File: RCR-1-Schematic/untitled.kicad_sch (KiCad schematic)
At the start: 24 parts, among them J1 AC In, SW1 Chassis Safety, T1A Transformer_1P_SS, T1B Transformer_1P_2S

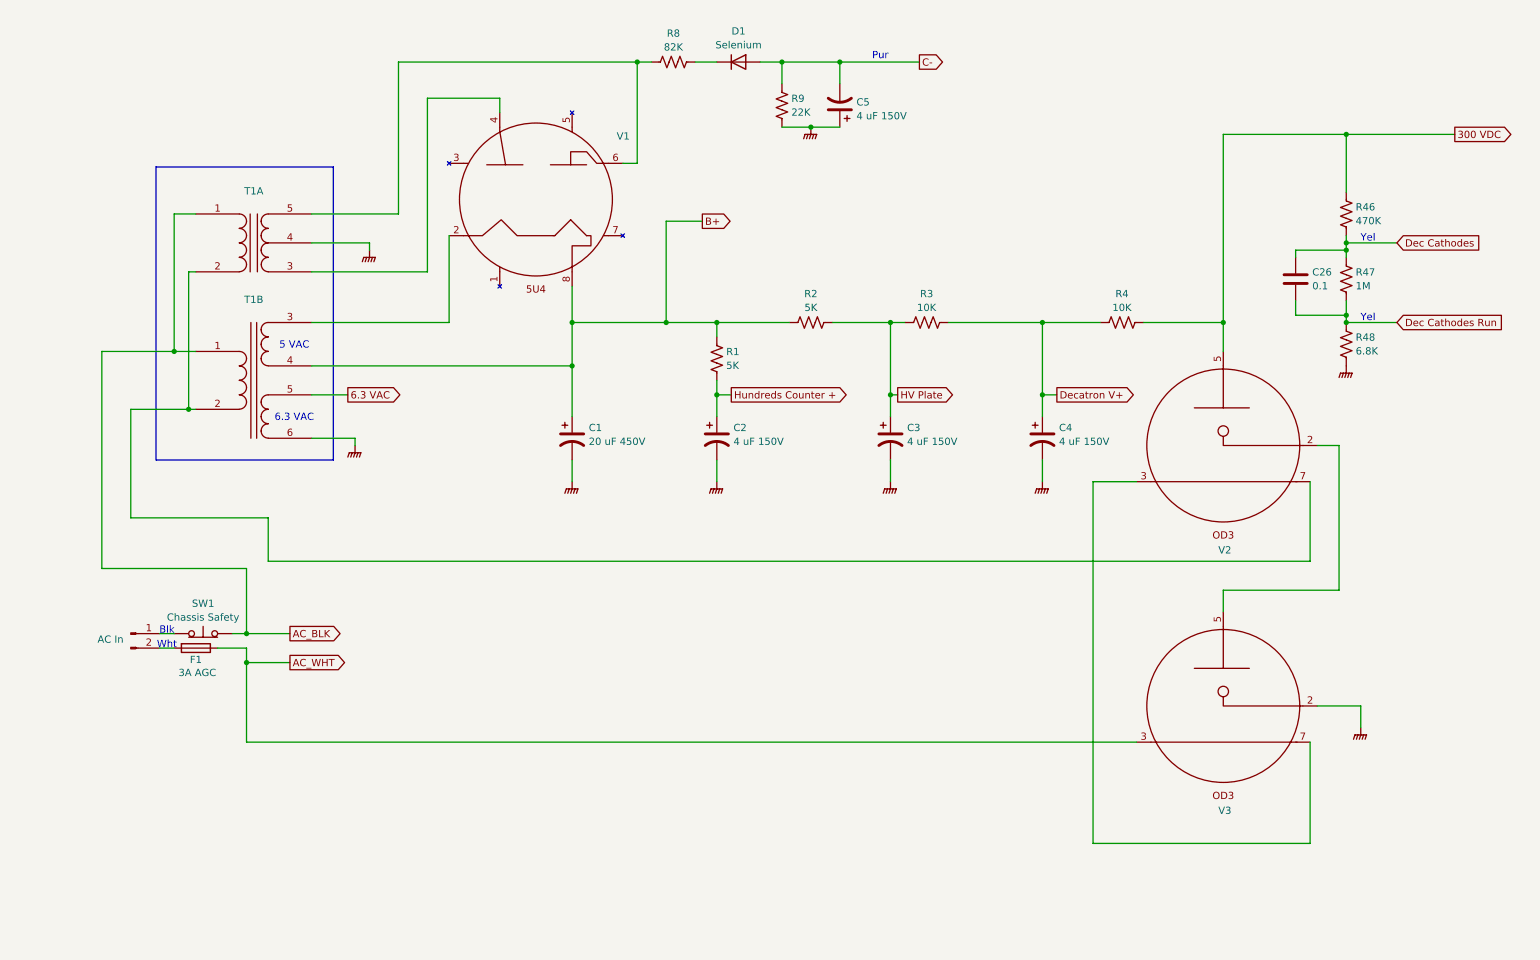
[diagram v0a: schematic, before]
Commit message: Add some oscilloscope screenshots, fixed some mistakes
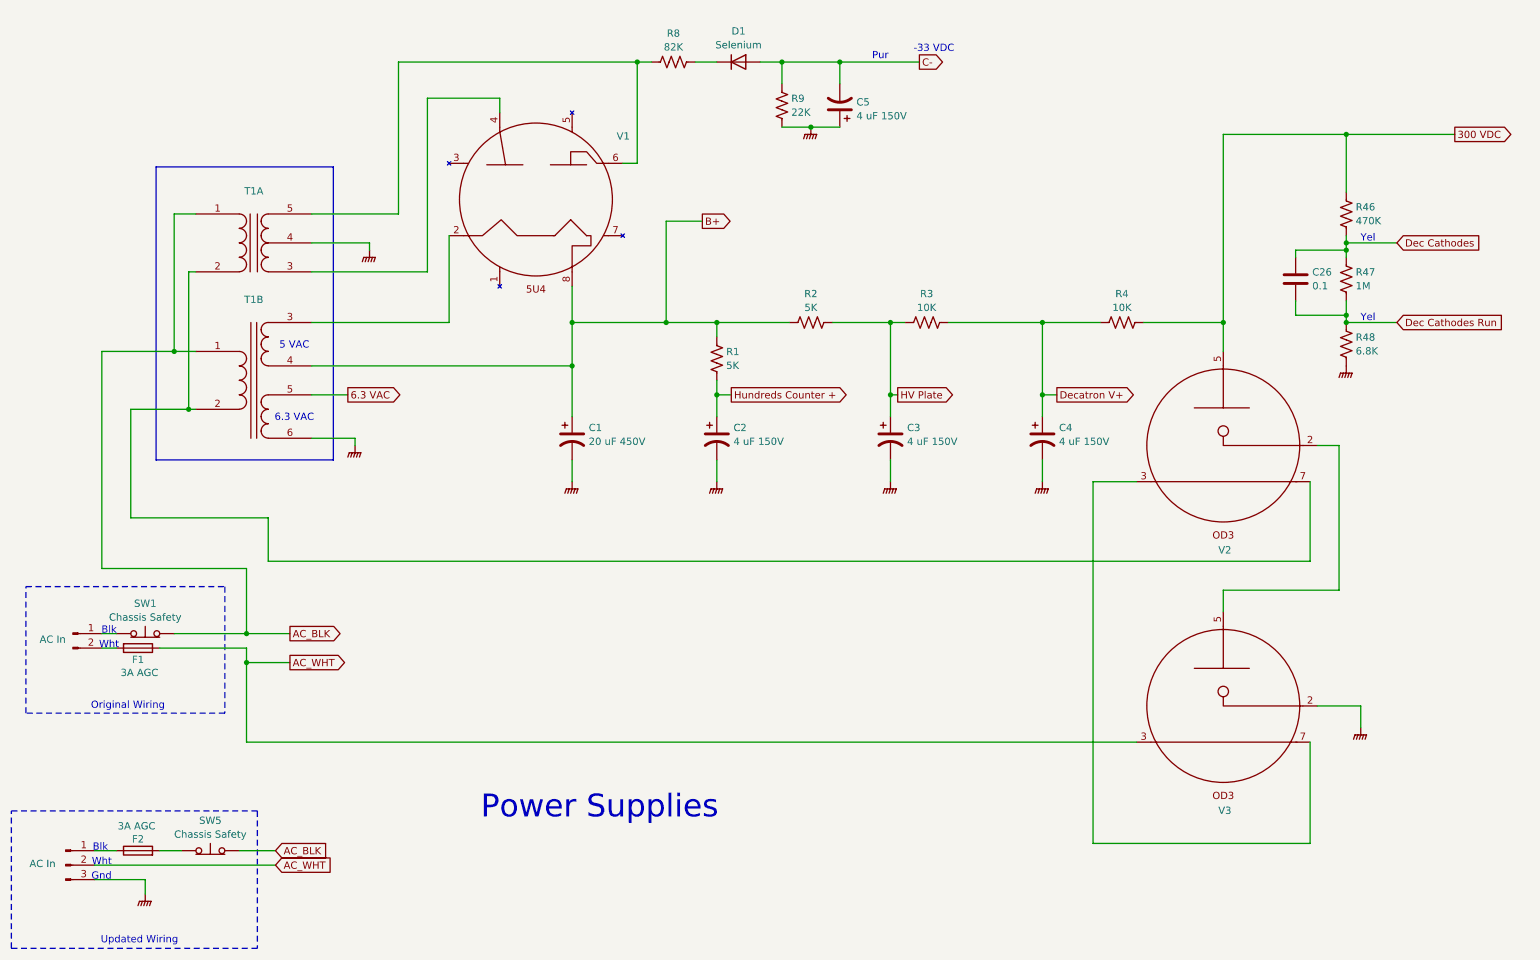
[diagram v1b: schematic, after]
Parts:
- added F2: 3A AGC, symbol Device:Fuse
- added J4: AC In, symbol Connector:Conn_01x03_Pin
- added SW5: Chassis Safety, symbol Switch:SW_Push_Open
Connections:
- net AC_BLK: now also SW5.2 (B)
- net AC_WHT: now also J4.2 (Pin_2)
- net GNDPWR: now also J4.3 (Pin_3)
- new net: F2.2, SW5.1 (A)
- new net: F2.1, J4.1 (Pin_1)
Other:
- note added: "-33 VDC"
- note added: "Gnd"
- note added: "Original Wiring"
- note added: "Power Supplies"
- note added: "Updated Wiring"
- moved on the sheet: F1, SW1

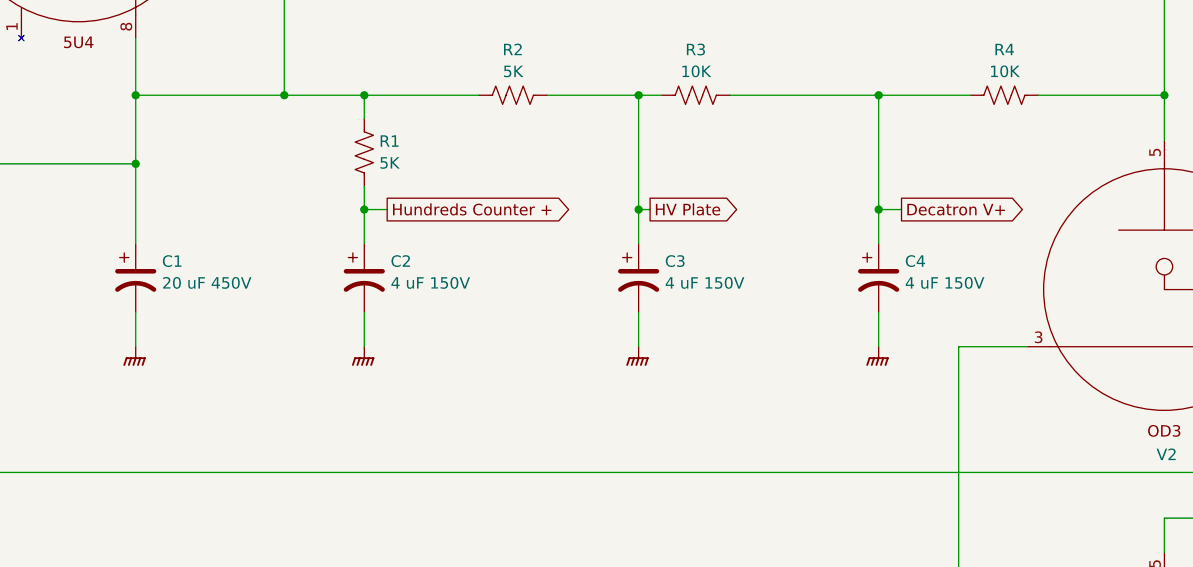
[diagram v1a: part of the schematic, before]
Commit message: Fix cap values in power supply
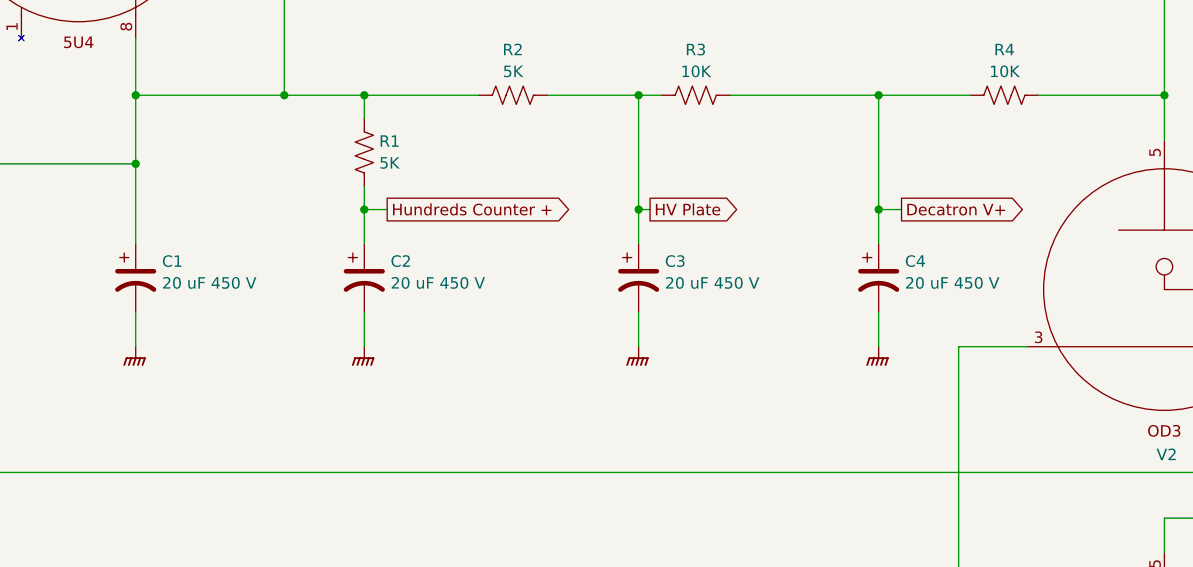
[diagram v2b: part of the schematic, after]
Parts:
- C1: value 20 uF 450V -> 20 uF 450 V
- C2, C3, C4: value 4 uF 150V -> 20 uF 450 V
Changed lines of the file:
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@@
 			)
 		)
-		(property "Value" "20 uF 450V"
+		(property "Value" "20 uF 450 V"
 			(at 118.491 92.0171 0)
 			(effects
@@
 			)
 		)
-		(property "Value" "4 uF 150V"
+		(property "Value" "20 uF 450 V"
 			(at 174.371 92.0171 0)
 			(effects
@@
 			)
 		)
-		(property "Value" "4 uF 150V"
+		(property "Value" "20 uF 450 V"
 			(at 143.891 92.0171 0)
 			(effects
@@
 			)
 		)
-		(property "Value" "4 uF 150V"
+		(property "Value" "20 uF 450 V"
 			(at 201.041 92.0171 0)
 			(effects

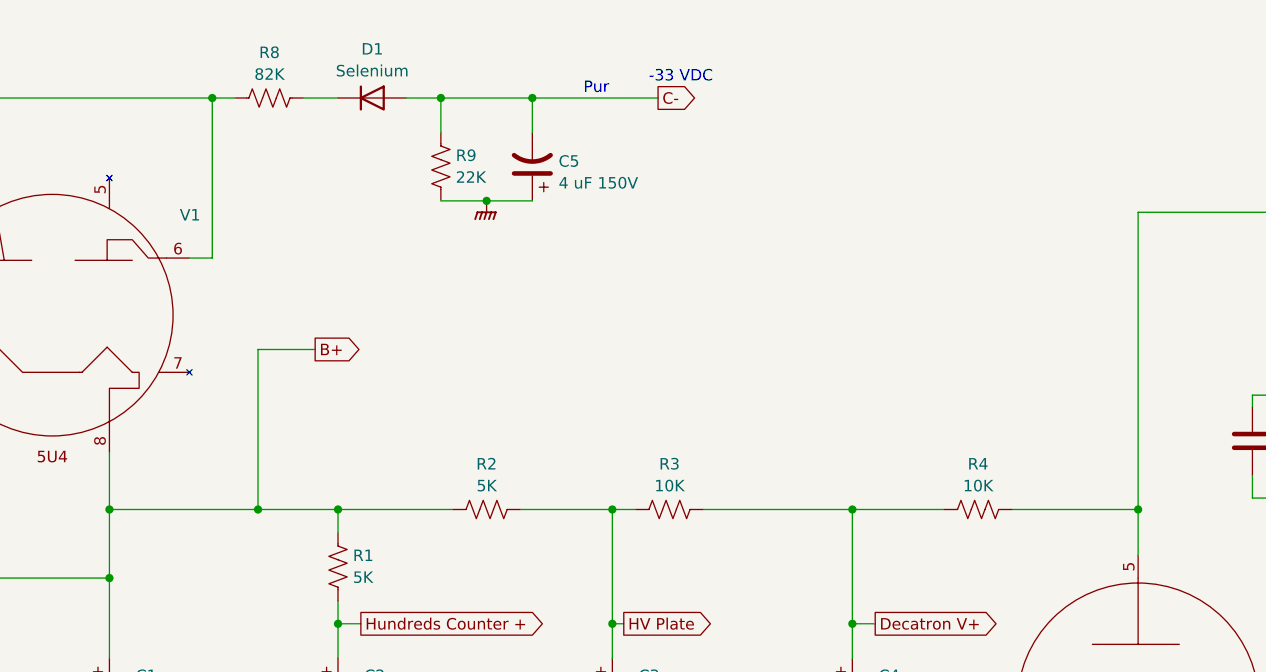
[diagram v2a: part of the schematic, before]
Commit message: Update schematic and README to reflect changes/updates
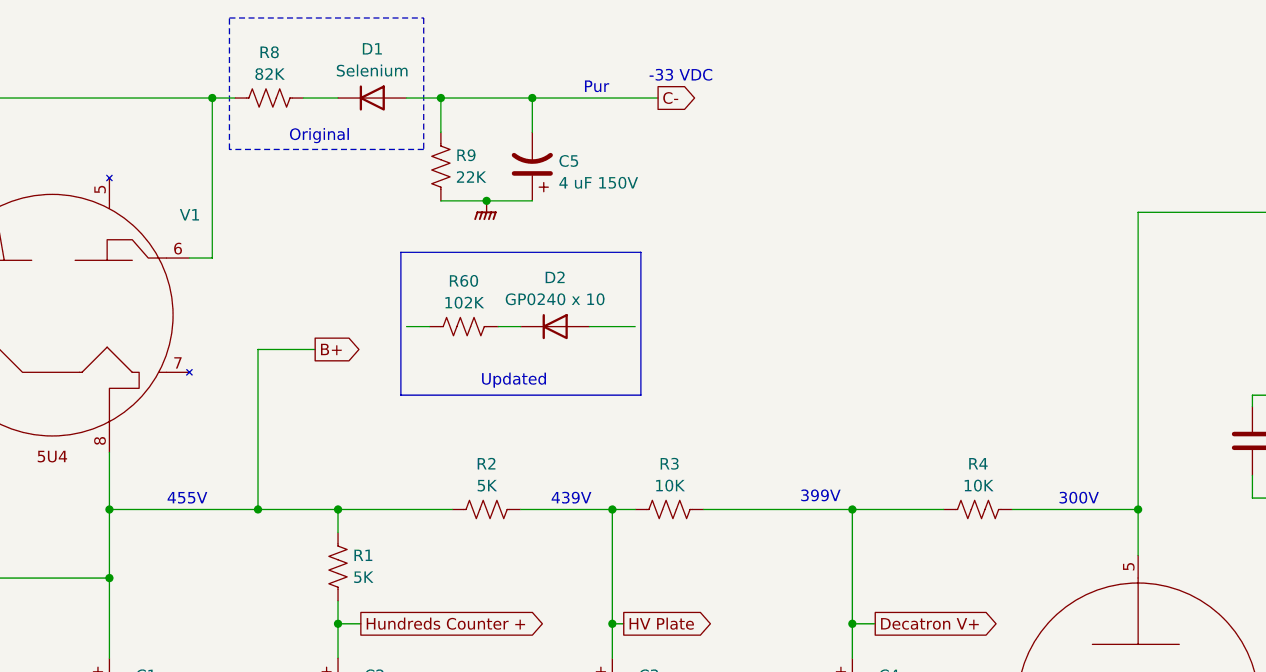
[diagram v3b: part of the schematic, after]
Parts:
- added D2: GP0240 x 10, symbol Device:D
- added R60: 102K, symbol Device:R_US
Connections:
- new net: D2.1 (K), R60.2
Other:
- note added: "300V"
- note added: "399V"
- note added: "439V"
- note added: "455V"
- note added: "Original"
- note added: "Updated"
